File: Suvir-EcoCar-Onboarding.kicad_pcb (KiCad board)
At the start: 2 copper layers, 100.7 x 55.7 mm, 54 parts, among them J1 Conn_01x04_Pin, J2 USB_B_Micro, J3 Conn_01x04_Pin, J4 Conn_01x04_Pin, J5 Conn_01x04_Pin, SW1 SW_SPDT, U1 STM32F103C8Tx, U2 AMS1117-3.3, U6 NHD-C0220BIZ, Y1 16MHz

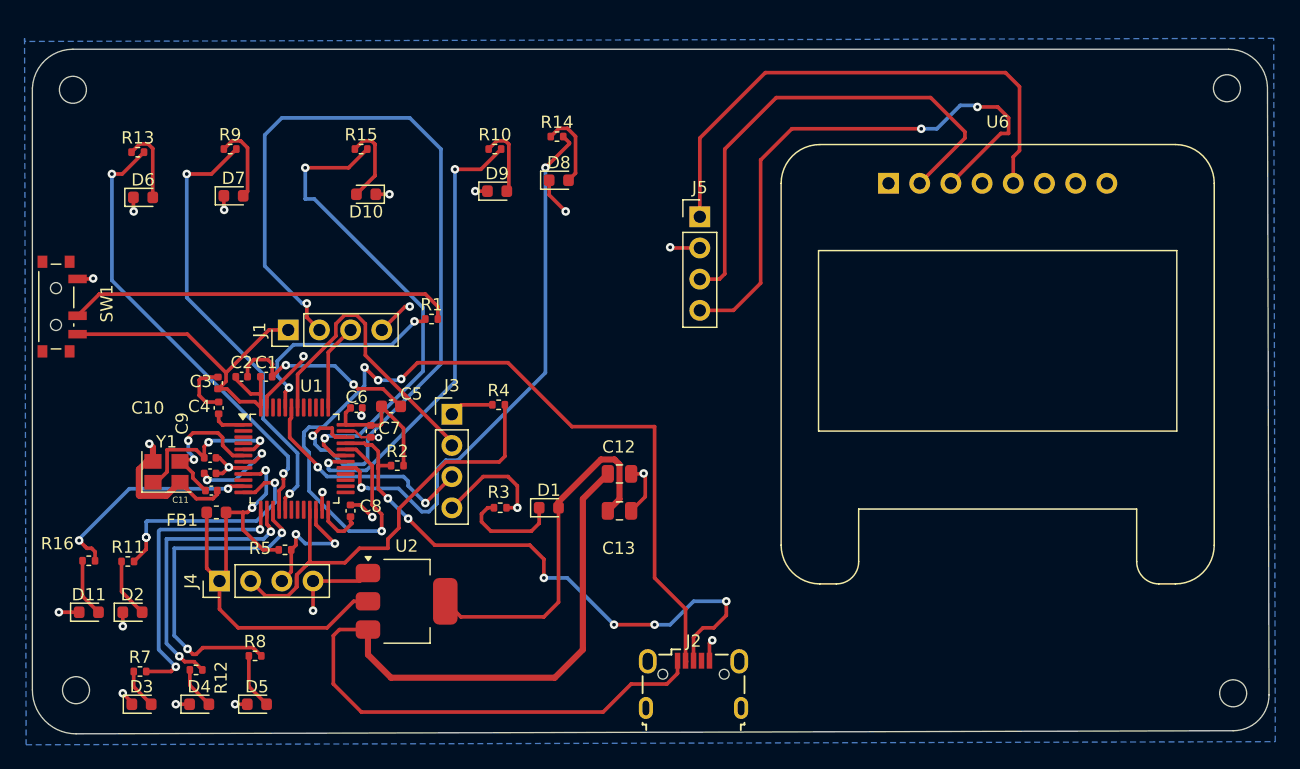
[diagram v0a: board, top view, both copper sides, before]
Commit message: made changes wrt routing
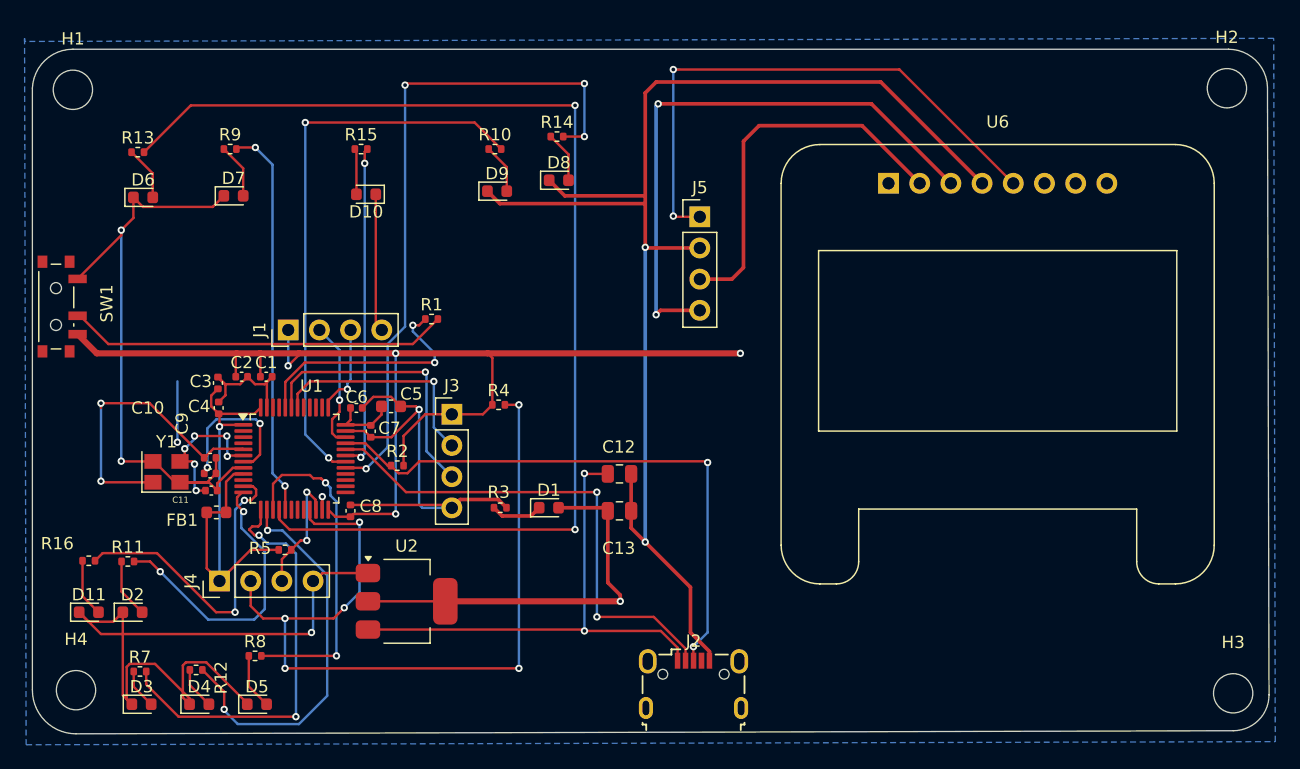
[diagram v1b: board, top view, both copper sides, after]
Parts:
- H1, H2, H3, H4: footprint MountingHole:MountingHole_2.2mm_M2 -> MountingHole:MountingHole_3.2mm_M3
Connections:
- net Net-(J3-Pin_3) renamed /USART1_RX
- net Net-(J4-Pin_3) renamed /I2C2_SDA
- C1 pad 2: Net-(C1-Pad2) -> GND
- C2 pad 2: Net-(C1-Pad2) -> GND
- C3 pad 2: Net-(C1-Pad2) -> GND
- C4 pad 2: Net-(C1-Pad2) -> GND
- C5 pad 2: Net-(C1-Pad2) -> GND
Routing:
- net GND: track 73.0 -> 289.1 mm, vias 24 -> 8
- net /SWDIO: track 71.2 -> 10.6 mm, vias 2 -> 1
- net Net-(U1-PA6): track 37.0 -> 96.4 mm
- net +3.3V: track 122.5 -> 174.1 mm, vias 2 -> 6
- net /USB_D-: track 75.7 -> 41.3 mm, vias 4 -> 2
- net VBUS: track 74.7 -> 41.6 mm, vias 0 -> 2
- net /I2C2_SCL: track 37.6 -> 68.7 mm, vias 0 -> 6
- net Net-(C1-Pad2): track 21.4 -> 0.00 mm, vias 2 -> 0
- net Net-(U1-PA10): track 39.7 -> 26.7 mm
- net /HSE_IN: track 14.0 -> 24.8 mm
- net Net-(U1-PA3): track 24.1 -> 34.5 mm
- net Net-(U1-PA8): track 45.1 -> 55.0 mm, vias 2 -> 4
- net /I2C1_SCL_OLED: track 40.5 -> 31.1 mm
- net Net-(U1-PA9): track 37.0 -> 46.5 mm
- net Net-(U1-PA4): track 23.0 -> 31.7 mm
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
